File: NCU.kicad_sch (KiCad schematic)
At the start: 3 parts, among them J1 RJ45, J2 USB_B, J3 Micro_SD_Card

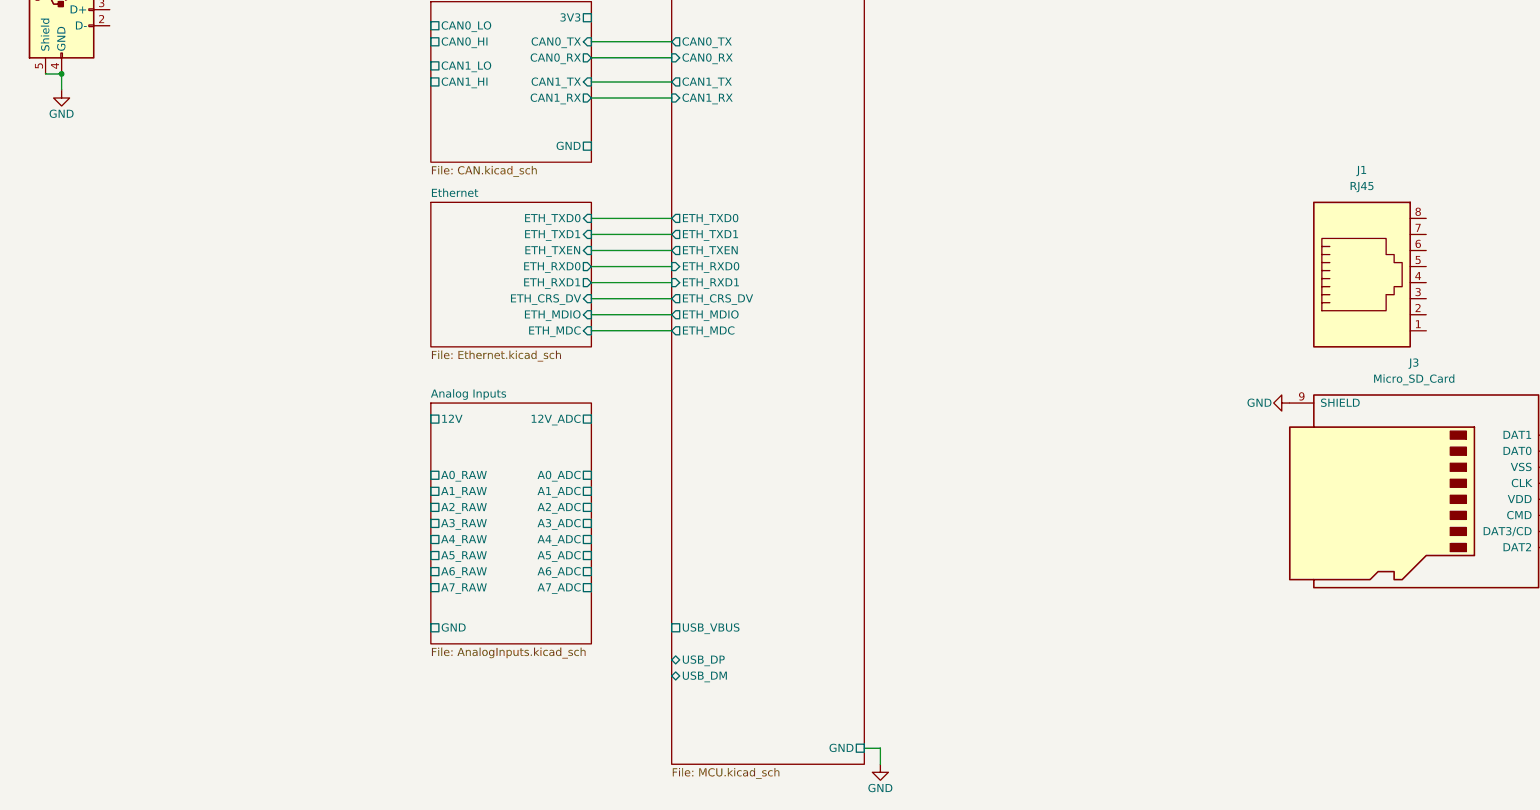
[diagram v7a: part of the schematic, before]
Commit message: added lib to project and added molex superseal connector
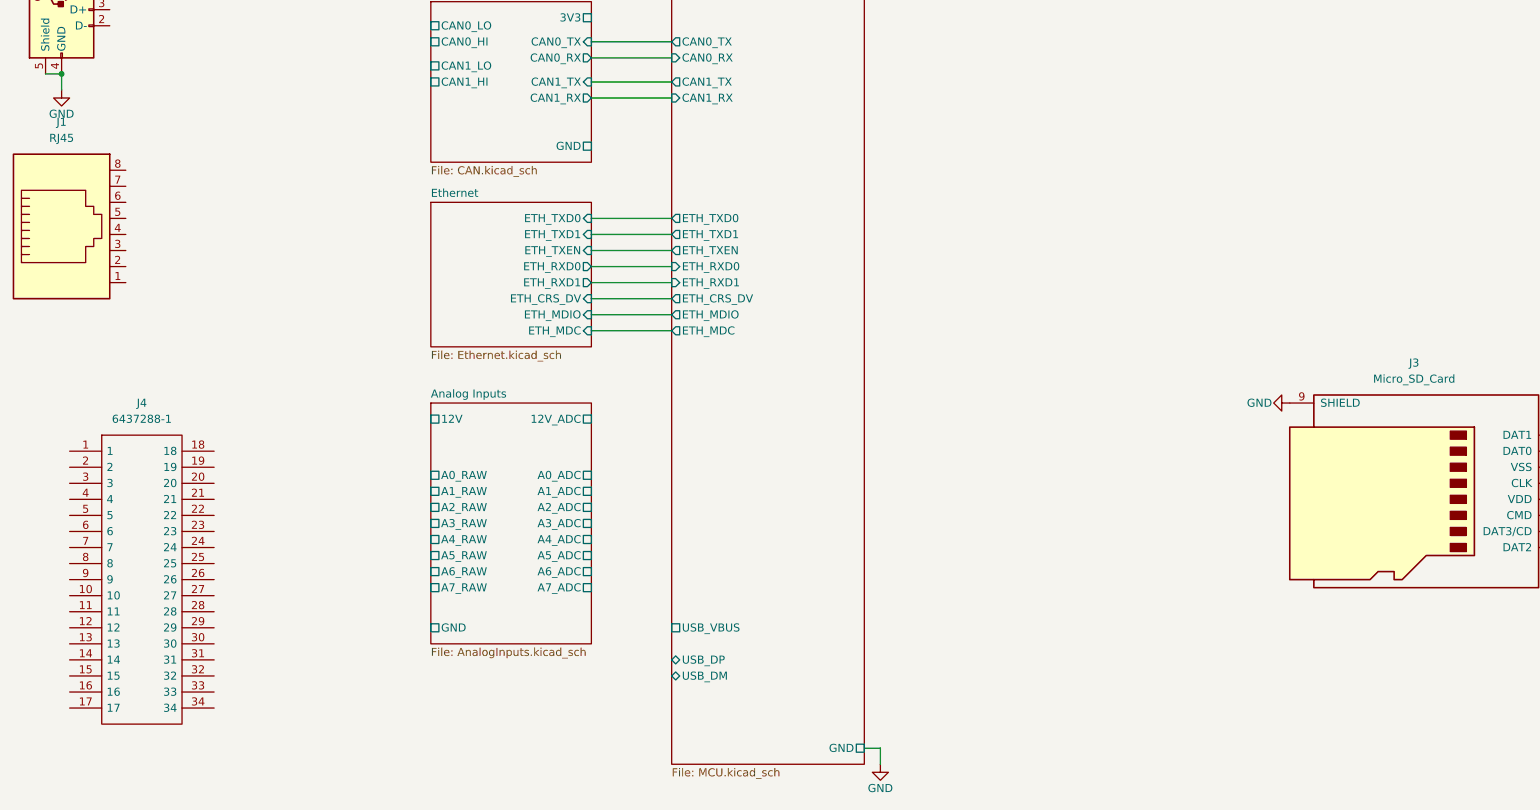
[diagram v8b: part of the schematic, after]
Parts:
- added J4: 6437288-1, 6437288-1, symbol 0_SamacSys_Parts:6437288-1
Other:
- moved on the sheet: J1
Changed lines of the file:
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@@
 	(symbol
 		(lib_id "Connector:RJ45")
-		(at 236.22 101.6 0)
+		(at 30.48 93.98 0)
 		(unit 1)
 		(exclude_from_sim no)
@@
 		(fields_autoplaced yes)
 		(property "Reference" "J1"
-			(at 236.22 83.82 0)
+			(at 30.48 76.2 0)
 			(effects
 				(font
@@
 		)
 		(property "Value" "RJ45"
-			(at 236.22 86.36 0)
+			(at 30.48 78.74 0)
 			(effects
 				(font
@@
 		)
 		(property "Footprint" "Connector_RJ:RJ45_Hanrun_HR911105A_Horizontal"
-			(at 236.22 100.965 90)
+			(at 30.48 93.345 90)
 			(effects
 				(font
@@
 		)
 		(property "Datasheet" "~"
-			(at 236.22 100.965 90)
+			(at 30.48 93.345 90)
 			(effects
 				(font
@@
 		)
 		(property "Description" "RJ connector, 8P8C (8 positions 8 connected)"
-			(at 236.22 101.6 0)
+			(at 30.48 93.98 0)
 			(effects
 				(font
@@
 					(unit 1)
 				)
+			)
+		)
+	)
+	(symbol
+		(lib_id "0_SamacSys_Parts:6437288-1")
+		(at 31.75 128.27 0)
+		(unit 1)
+		(exclude_from_sim no)
+		(in_bom yes)
+		(on_board yes)
+		(dnp no)
+		(fields_autoplaced yes)
+		(property "Reference" "J4"
+			(at 43.18 120.65 0)
+			(effects
+				(font
+					(size 1.27 1.27)
+				)
+			)
+		)
+		(property "Value" "6437288-1"
+			(at 43.18 123.19 0)
+			(effects
+				(font
+					(size 1.27 1.27)
+				)
+			)
+		)
+		(property "Footprint" "6437288-1"
+			(at 50.8 125.73 0)
+			(effects
+				(font
+					(size 1.27 1.27)
+				)
+				(justify left)
+				(hide yes)
+			)
+		)
+		(property "Datasheet" "https://www.te.com/commerce/DocumentDelivery/DDEController?Action=srchrtrv&DocNm=1-1773950-7&DocType=Data%20Sheet&DocLang=English&PartCntxt=6437288-1&DocFormat=pdf"
+			(at 50.8 128.27 0)
+			(effects
+				(font
+					(size 1.27 1.27)
+				)
+				(justify left)
+				(hide yes)
+			)
+		)
+		(property "Description" "Body Features: Primary Product Color Black | Configuration Features: Number of Positions 34 | Number of Signal Positions 34 | Number of Sections 1 | Number of Rows 4 | PCB Mount Orientation Horizontal | Contact Features: Contact Size 1mm | Contact Type Pin | Mating Pin Diameter .039 INCH | Mating Pin Diameter 1 MM | Contact Mating Area Plating Material Gold | Dimensions: Profile Height from PCB 1.098 INCH | Connector Width 1.791 INCH | Connector Length 36.5 MM | Profile Height from PCB 27.9 MM | Connector W"
+			(at 31.75 128.27 0)
+			(effects
+				(font
+					(size 1.27 1.27)
+				)
+				(hide yes)
+			)
+		)
+		(property "Description_1" "Body Features: Primary Product Color Black | Configuration Features: Number of Positions 34 | Number of Signal Positions 34 | Number of Sections 1 | Number of Rows 4 | PCB Mount Orientation Horizontal | Contact Features: Contact Size 1mm | Contact Type Pin | Mating Pin Diameter .039 INCH | Mating Pin Diameter 1 MM | Contact Mating Area Plating Material Gold | Dimensions: Profile Height from PCB 1.098 INCH | Connector Width 1.791 INCH | Connector Length 36.5 MM | Profile Height from PCB 27.9 MM | Connector W"
+			(at 50.8 130.81 0)
+			(effects
+				(font
+					(size 1.27 1.27)
+				)
+				(justify left)
+				(hide yes)
+			)
+		)
+		(property "Height" ""
+			(at 50.8 133.35 0)
+			(effects
+				(font
+					(size 1.27 1.27)
+				)
+				(justify left)
+				(hide yes)
+			)
+		)
+		(property "Mouser Part Number" "571-6437288-1"
+			(at 50.8 135.89 0)
+			(effects
+				(font
+					(size 1.27 1.27)
+				)
+				(justify left)
+				(hide yes)
+			)
+		)
+		(property "Mouser Price/Stock" "https://www.mouser.co.uk/ProductDetail/TE-Connectivity/6437288-1?qs=WBj8811fzwGYtKR8aBSJZw%3D%3D"
+			(at 50.8 138.43 0)
+			(effects
+				(font
+					(size 1.27 1.27)
+				)
+				(justify left)
+				(hide yes)
+			)
+		)
+		(property "Manufacturer_Name" "TE Connectivity"
+			(at 50.8 140.97 0)
+			(effects
+				(font
+					(size 1.27 1.27)
+				)
+				(justify left)
+				(hide yes)
+			)
+		)
+		(property "Manufacturer_Part_Number" "6437288-1"
+			(at 50.8 143.51 0)
+			(effects
+				(font
+					(size 1.27 1.27)
+				)
+				(justify left)
+				(hide yes)
+			)
+		)
+		(pin "11"
+		)
+		(pin "17"
+		)
+		(pin "1"
+		)
+		(pin "4"
+		)
+		(pin "12"
+		)
+		(pin "8"
+		)
+		(pin "14"
+		)
+		(pin "16"
+		)
+		(pin "9"
+		)
+		(pin "13"
+		)
+		(pin "7"
+		)
+		(pin "33"
+		)
+		(pin "22"
+		)
+		(pin "6"
+		)
+		(pin "10"
+		)
+		(pin "15"
+		)
+		(pin "2"
+		)
+		(pin "3"
+		)
+		(pin "5"
+		)
+		(pin "23"
+		)
+		(pin "24"
+		)
+		(pin "25"
+		)
+		(pin "26"
+		)
+		(pin "19"
+		)
+		(pin "21"
+		)
+		(pin "27"
+		)
+		(pin "28"
+		)
+		(pin "30"
+		)
+		(pin "18"
+		)
+		(pin "20"
+		)
+		(pin "29"
+		)
+		(pin "31"
+		)
+		(pin "32"
+		)
+		(pin "34"
+		)
+		(instances
+			(project ""
+				(path "/3aee14c3-5480-4f7c-989e-3fef81779034"
+					(reference "J4")
+					(unit 1)
+				)
